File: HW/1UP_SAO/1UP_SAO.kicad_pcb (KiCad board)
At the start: 2 copper layers, 48 x 48 mm, 12 parts, among them X1 Badgelife_sao_connector_v169b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

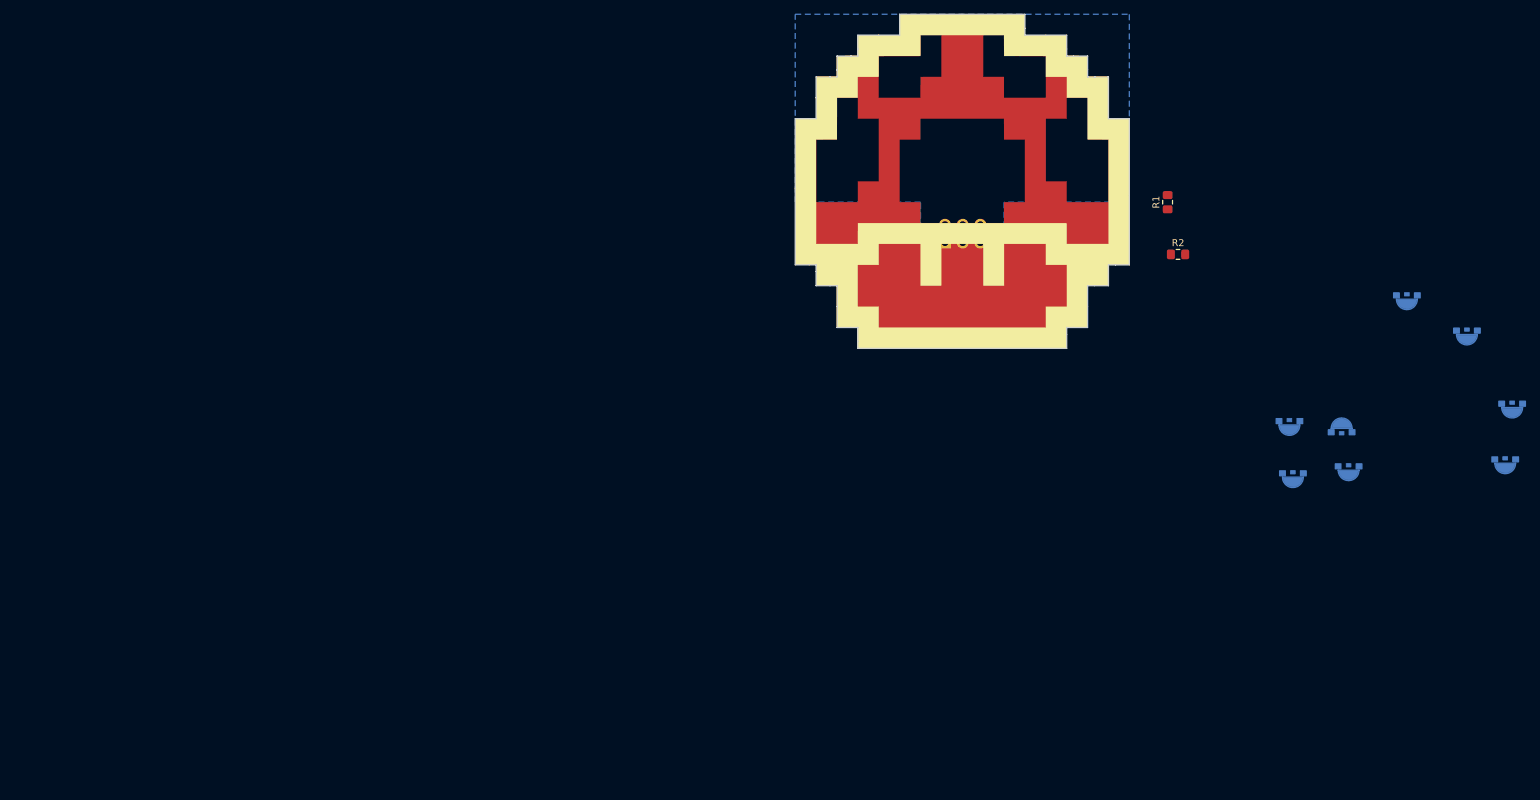
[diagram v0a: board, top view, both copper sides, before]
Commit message: Art done for now. updated PCB with footprints and parts. updated library stuff to be relative paths
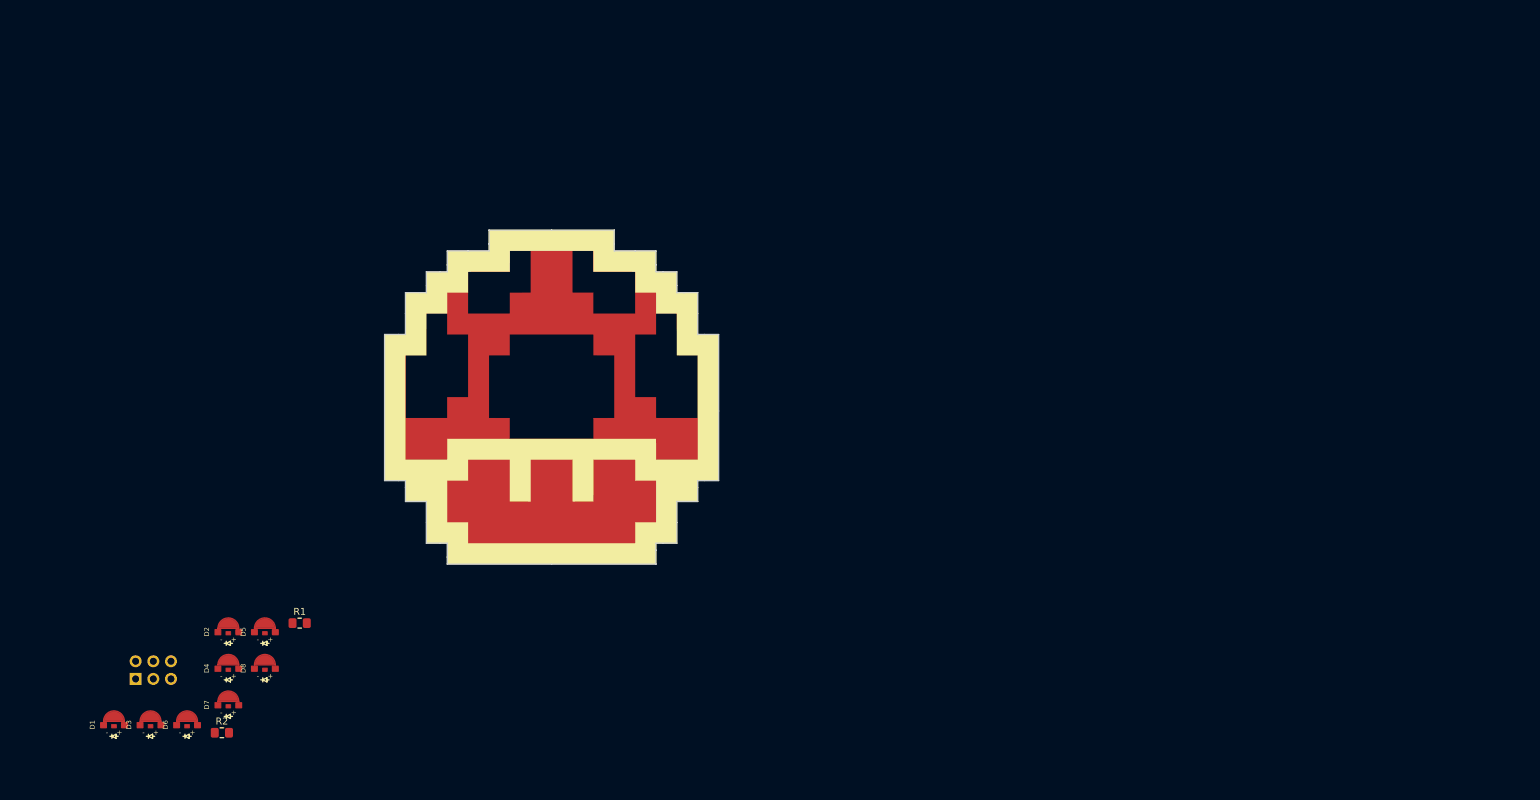
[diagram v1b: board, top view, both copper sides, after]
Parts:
- removed Ref**: Val**, 1UP_SAO:1UP_layers
- added G*** (x5): LOGO, LOGO, F.Cu at (100.0, 100.0)
- D1, D2, D3, D4, D5, D6, D7, D8: moved to F.Cu
- moved D6 193.2 mm to (47.6, 147.1)
- moved D7 185.9 mm to (53.6, 144.2)
- moved D8 183.2 mm to (58.8, 139.0)
- moved D3 176.2 mm to (42.4, 147.1), turned to 0 degrees
- moved D1 173.2 mm to (37.1, 147.1)
- moved D5 171.0 mm to (58.8, 133.7)
- moved D4 163.5 mm to (53.6, 139.0)
- moved D2 155.4 mm to (53.6, 133.7)
- moved R2 153.6 mm to (52.6, 148.2)
- moved R1 138.6 mm to (63.8, 132.5), turned to 0 degrees
- moved X1 132.1 mm to (42.7, 139.2)
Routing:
- removed copper zone on B.Cu, net GND
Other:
- net class Default: via_dia 0.8 -> 0.6
- rule pad_to_mask_clearance: 0.051 -> 0.2

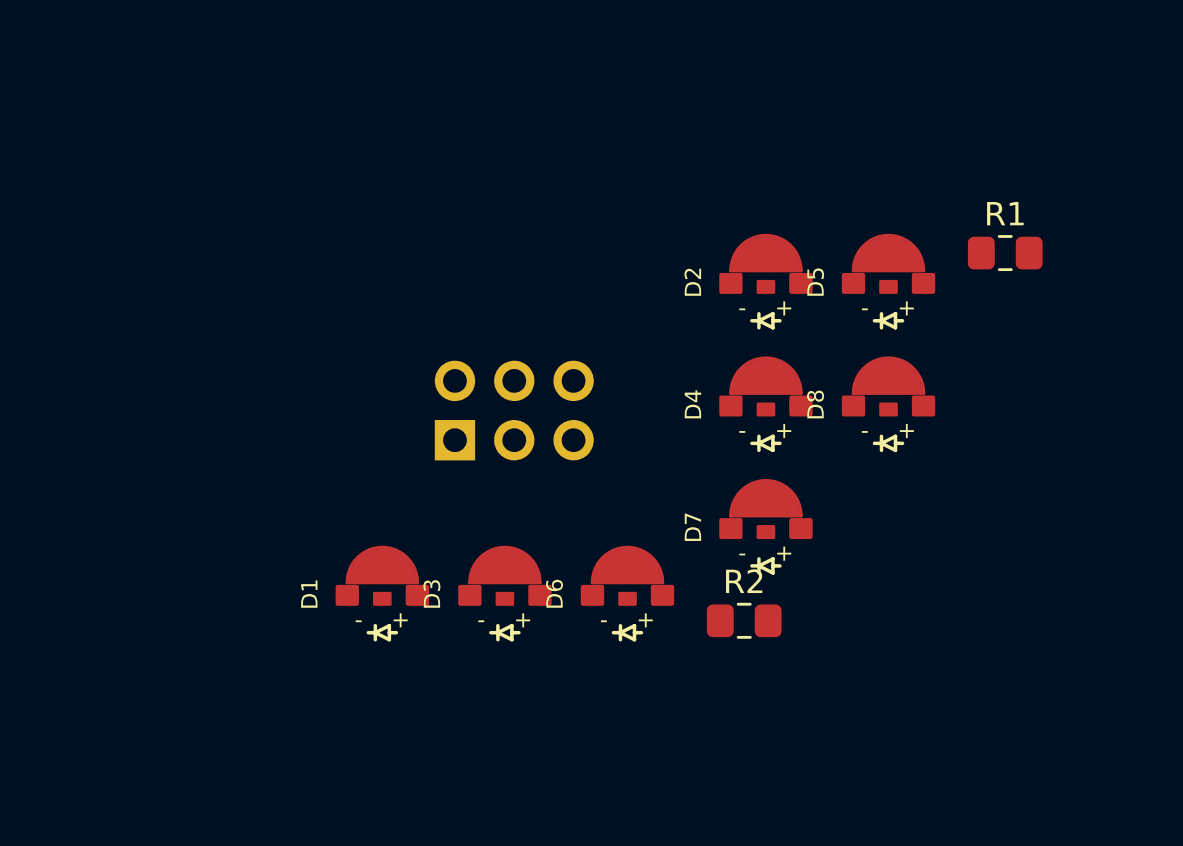
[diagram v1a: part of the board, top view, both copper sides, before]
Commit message: moved parts to back layer
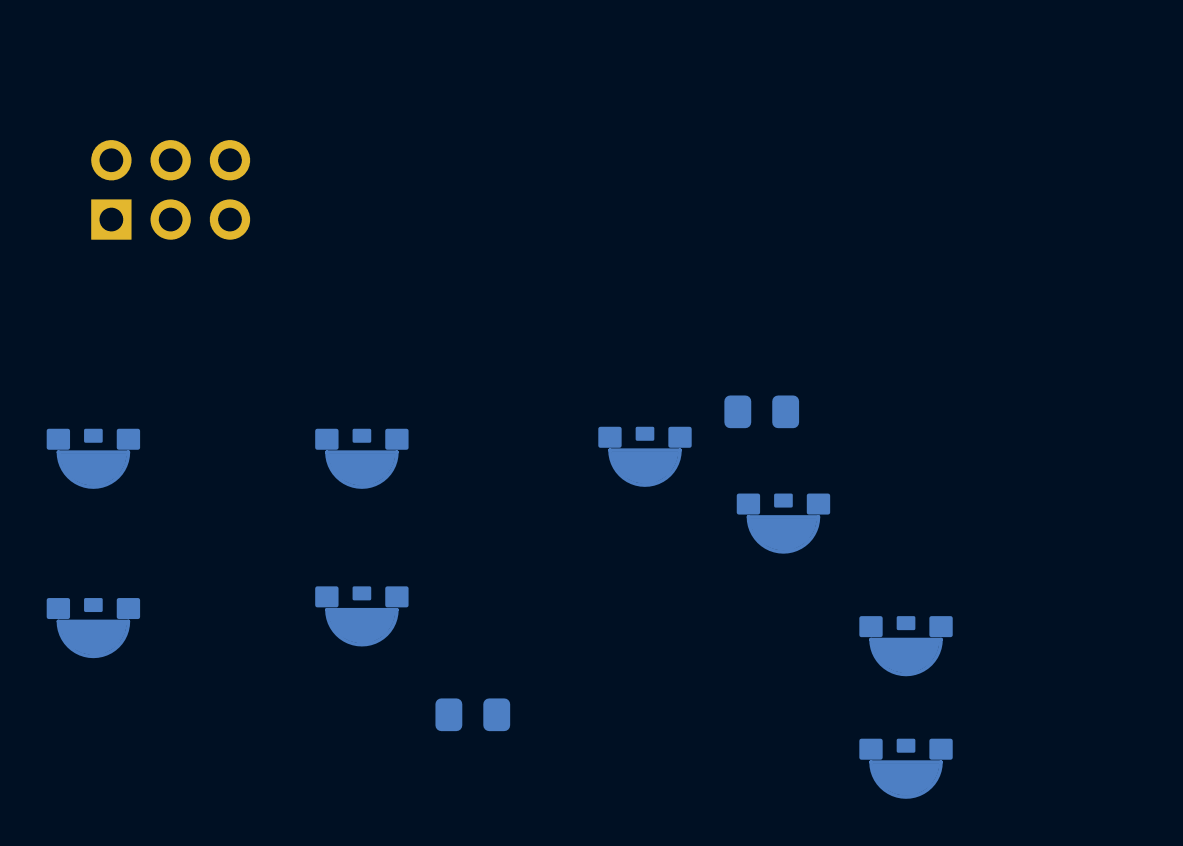
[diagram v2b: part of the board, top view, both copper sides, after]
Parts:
- removed the G*** at (100.0, 100.0) (x4)
- added G*** (x4): LOGO, LOGO, F.Cu at (100.0, 100.0)
- D1, D2, D3, D4, D5, D6, D7, D8, R1, R2: moved to B.Cu
- moved R1 30.2 mm to (41.0, 152.2)
- moved D4 30.1 mm to (24.8, 147.8)
- moved D2 22.0 mm to (36.2, 147.2)
- moved D5 20.1 mm to (59.6, 153.8)
- moved X1 17.5 mm to (28.0, 129.8)
- moved D1 14.0 mm to (24.8, 140.5)
- moved D8 9.58 mm to (59.6, 148.5)
- moved D3 8.99 mm to (36.2, 140.5)
- moved R2 8.98 mm to (53.4, 139.3)
- moved D6 6.71 mm to (48.4, 140.4)
- moved D7 1.21 mm to (54.3, 143.3)

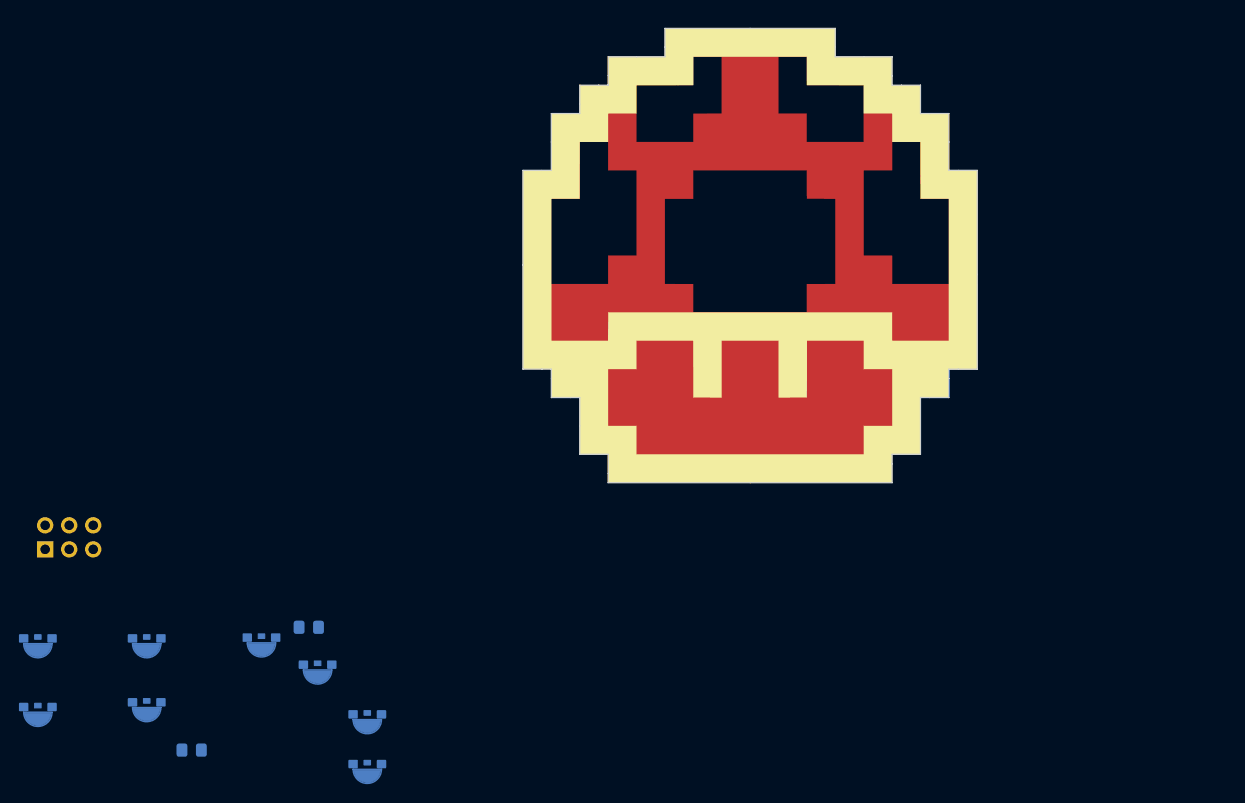
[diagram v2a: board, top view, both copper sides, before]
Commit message: added VCC net. Fixed Footprint for LEDs. Layout some LEDs
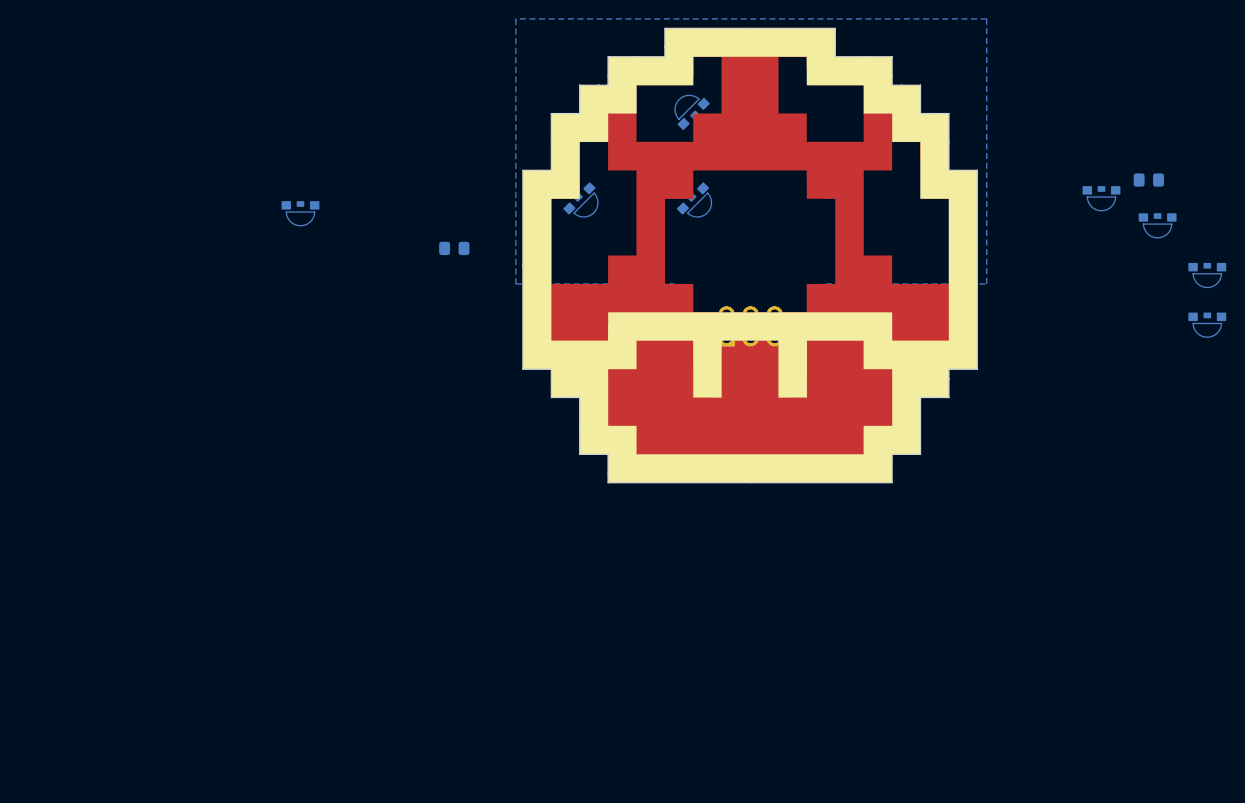
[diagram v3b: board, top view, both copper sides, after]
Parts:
- removed the G*** at (100.0, 100.0) (x5)
- added G***: F.Mask, LOGO, F.Cu at (100.0, 100.0)
- added G***: B.Silk, LOGO, F.Cu at (100.0, 100.0)
- added G***: B.Cu, LOGO, F.Cu at (100.0, 100.0)
- added G*** (x2): LOGO, LOGO, F.Cu at (100.0, 100.0)
- moved D5 100.5 mm to (148.3, 106.5)
- moved D6 100.5 mm to (137.1, 93.2)
- moved D7 100.5 mm to (143.1, 96.0)
- moved D8 100.5 mm to (148.3, 101.3)
- moved R2 100.5 mm to (142.1, 92.0)
- moved D1 88.7 mm to (94.0, 85.0), turned to 225 degrees
- moved D2 78.6 mm to (94.0, 94.0), turned to 45 degrees
- moved X1 75.4 mm to (100.0, 107.5)
- moved D3 65.2 mm to (82.0, 94.0), turned to 45 degrees
- moved D4 59.8 mm to (52.5, 94.8)
- moved R1 59.8 mm to (68.8, 99.2)
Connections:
- net Net-(R1-Pad1) renamed VCC
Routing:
- added copper zone on B.Cu, net GND
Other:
- net class Default: clearance 0.2 -> 0.1524; trace_width 0.25 -> 0.2032
- rule pad_to_mask_clearance: 0.2 -> 0.1524
- rule trace_clearance: 0.2 -> 0.1524

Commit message: moving stuff around
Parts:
- moved D5 47.5 mm to (106.0, 85.0), turned to 135 degrees
- moved De 43.3 mm to (105.0, 102.0), turned to 225 degrees
- moved R2 40.0 mm to (102.2, 89.0), turned to 90 degrees
- moved D7 37.1 mm to (106.0, 94.0), turned to 315 degrees
- moved R1 30.5 mm to (97.5, 89.0), turned to 90 degrees
- moved D4 28.0 mm to (80.2, 98.5), turned to 90 degrees
- moved D6 19.1 mm to (118.0, 94.0), turned to 315 degrees
- moved G*** 14.5 mm to (100.0, 114.5)
- moved D1 5.39 mm to (89.0, 83.0), turned to 45 degrees
- moved D3 4.32 mm to (85.0, 90.9), turned to 315 degrees
- moved D2 1.41 mm to (95.0, 95.0)
- moved X1 1.04 mm to (100.0, 108.5)
- renumbered D8 to De
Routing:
- net VCC: track 0.00 -> 22.0 mm
- net Net-(D1-Pad2): track 0.00 -> 9.03 mm
